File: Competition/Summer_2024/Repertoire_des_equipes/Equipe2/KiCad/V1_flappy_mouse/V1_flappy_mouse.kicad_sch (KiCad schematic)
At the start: 0 parts

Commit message: Push des changements fait
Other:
- note added: "Tâche à faire: - Moitier de capacitive touche - Accéléromètre ❎ - Switch ❎ - Connexion Ordinateur (déjà sur le ESP32) ❎ - Alimentation* (déjà sur le ESP32) ❎ - Micro SD card reader"
- note removed: "Tâche à faire: - Moitier de capacitive touche - Accéléromètre - Switch - Connexion Ordinateur - Alimentation*"
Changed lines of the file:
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@@
 		)
 	)
-	(text "Tâche à faire:\n- Moitier de capacitive touche\n- Accéléromètre\n- Switch\n- Connexion Ordinateur\n- Alimentation*"
+	(text "Tâche à faire:\n- Moitier de capacitive touche \n- Accéléromètre ❎\n- Switch ❎ \n- Connexion Ordinateur (déjà sur le ESP32) ❎\n- Alimentation* (déjà sur le ESP32) ❎\n- Micro SD card reader"
 		(exclude_from_sim no)
-		(at 15.24 26.67 0)
+		(at 14.986 27.432 0)
 		(effects
 			(font

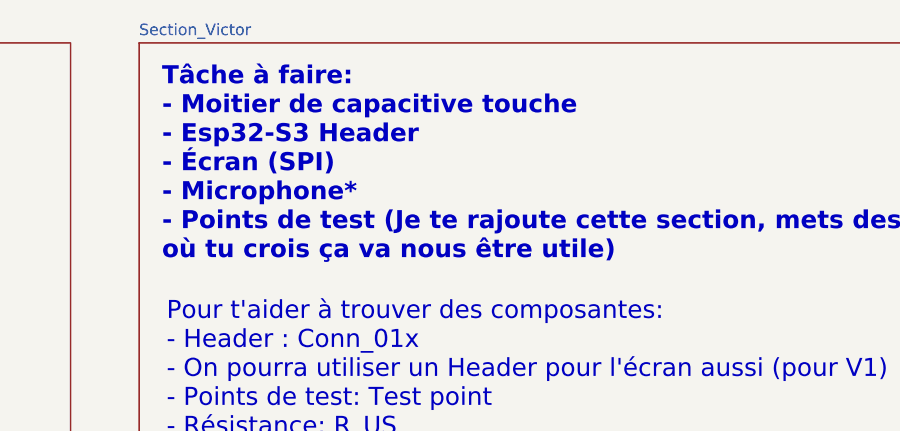
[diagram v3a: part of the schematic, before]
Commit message: add the component on the PCB
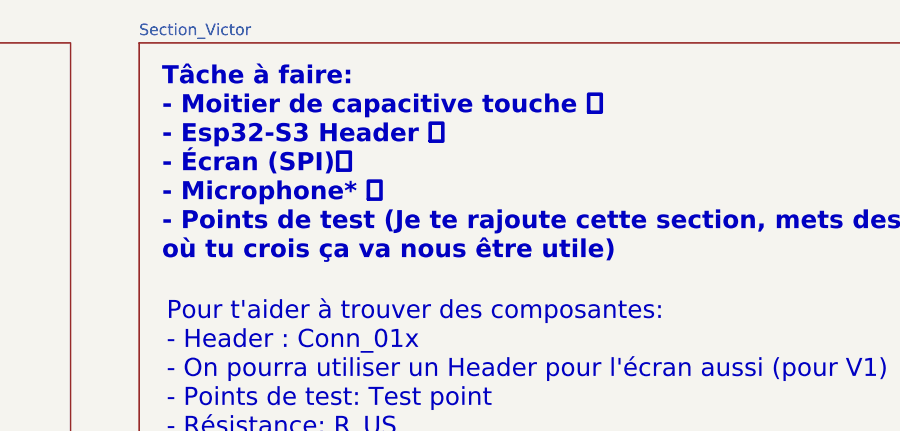
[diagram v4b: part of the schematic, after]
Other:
- note added: "Tâche à faire: - Moitier de capacitive touche ❎ - Esp32-S3 Header ❎ - Écran (SPI)❎ - Microphone* ❎ - Points de test (Je te rajoute cette section, mets des points de test où tu crois ça va nous être utile)"
- note removed: "Tâche à faire: - Moitier de capacitive touche - Esp32-S3 Header - Écran (SPI) - Microphone* - Points de test (Je te rajoute cette section, mets des points de test où tu crois ça va nous être utile)"
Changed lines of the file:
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@@
 		)
 	)
-	(text "Tâche à faire:\n- Moitier de capacitive touche\n- Esp32-S3 Header\n- Écran (SPI)\n- Microphone*\n- Points de test (Je te rajoute cette section, mets des points de test \noù tu crois ça va nous être utile)"
+	(text "Tâche à faire:\n- Moitier de capacitive touche ❎\n- Esp32-S3 Header ❎\n- Écran (SPI)❎\n- Microphone* ❎\n- Points de test (Je te rajoute cette section, mets des points de test \noù tu crois ça va nous être utile)"
 		(exclude_from_sim no)
 		(at 146.05 28.702 0)
